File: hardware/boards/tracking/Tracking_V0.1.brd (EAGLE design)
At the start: 44 x 44 mm, 37 parts, among them J1 CON_HEADER_PRG_AVR_ICSP-PTH, U1 ATMEGA328P-AU, U3 USD-SOCKETNEW

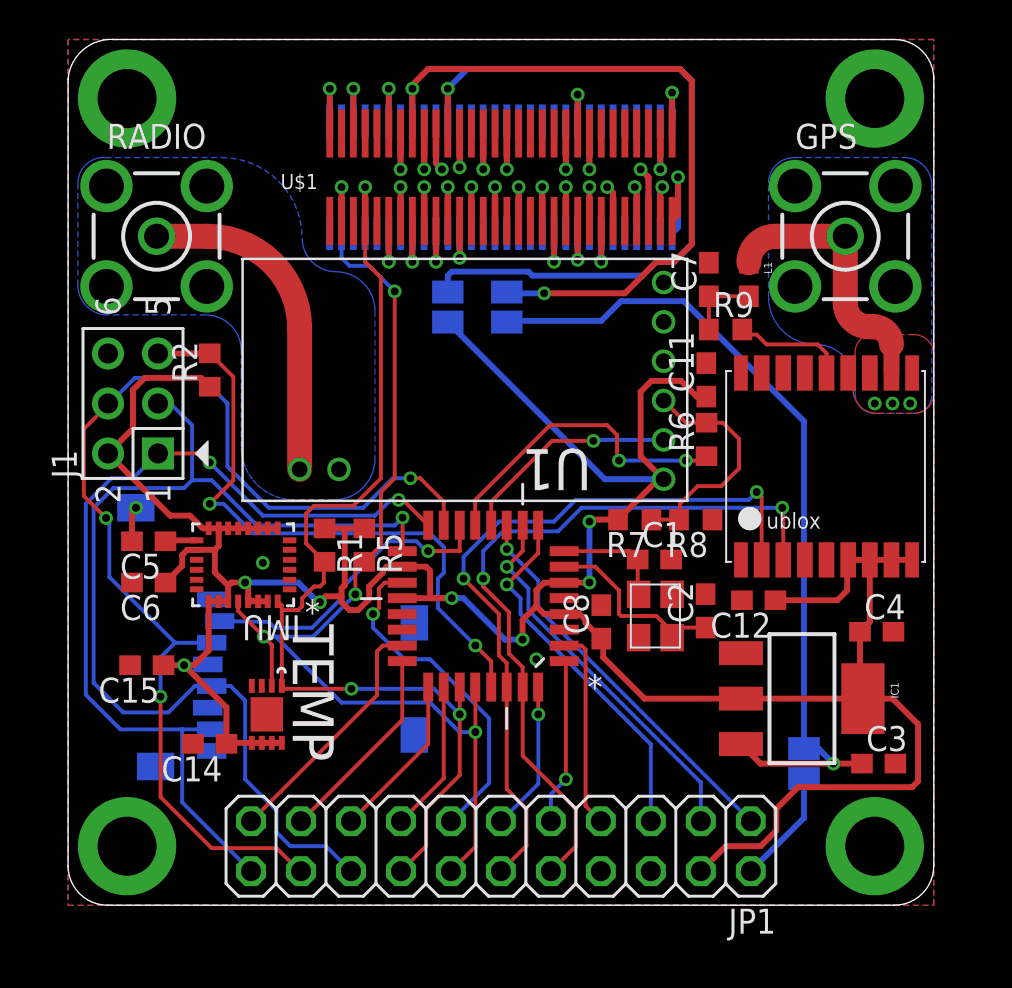
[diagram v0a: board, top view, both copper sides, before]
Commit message: Switched to right angle SMA connectors, created 3d render
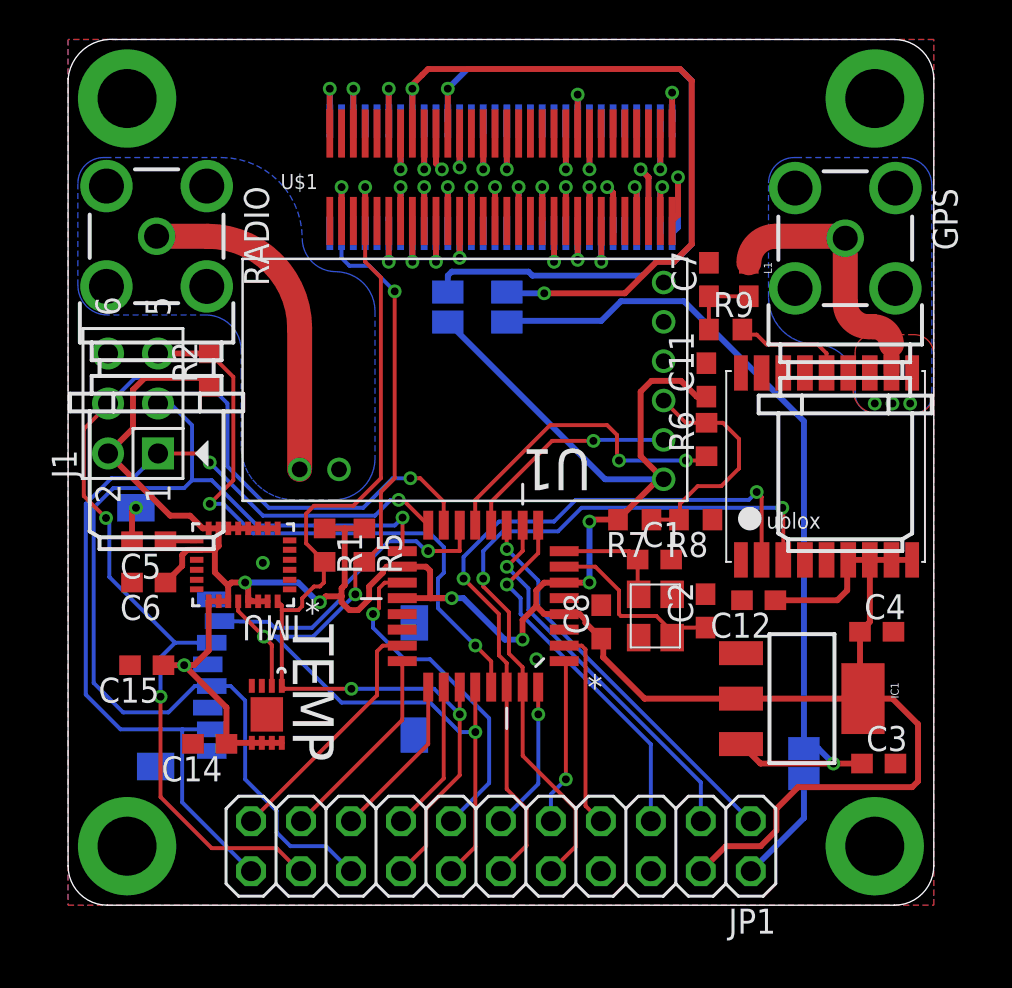
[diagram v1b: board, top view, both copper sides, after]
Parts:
- GPS, RADIO: value BU-SMA-V -> BU-SMA-G; device con-coax:BU-SMA-V -> con-coax:BU-SMA-G
- moved GPS 0.10 mm to (39.5, 33.9), turned to 270 degrees
- turned RADIO to 270 degrees
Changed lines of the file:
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@@
 <layer number="220" name="220bmp" color="21" fill="1" visible="no" active="no"/>
 <layer number="221" name="221bmp" color="22" fill="1" visible="no" active="no"/>
-<layer number="222" name="222bmp" color="23" fill="1" visible="no" active="no"/>
 <layer number="223" name="223bmp" color="24" fill="1" visible="no" active="no"/>
 <layer number="224" name="224bmp" color="25" fill="1" visible="no" active="no"/>
@@
 <element name="3.3V" library="jumper" package="SJ" value="" x="19.3" y="30.4" rot="MR90"/>
 <element name="U$4" library="Ava" package="UBLOX_MAX" value="UBLOX_MAX" x="38.6" y="22.5" rot="R270"/>
-<element name="GPS" library="con-coax" package="BU-SMA-V" value="BU-SMA-V" x="39.5" y="34">
-<attribute name="OC_NEWARK" value="unknown" x="31" y="36.3" size="1.778" layer="27" display="off"/>
-<attribute name="MPN" value="" x="31" y="36.3" size="1.778" layer="27" display="off"/>
-<attribute name="MF" value="" x="31" y="36.3" size="1.778" layer="27" display="off"/>
-<attribute name="OC_FARNELL" value="2144531" x="31" y="36.3" size="1.778" layer="27" display="off"/>
-</element>
 <element name="C12" library="rcl" package="C0603" value="100n" x="35.1" y="15.5" rot="R180">
 <attribute name="OC_FARNELL" value="2429362" x="55" y="13.3" size="1.778" layer="27" rot="R180" display="off"/>
@@
 <element name="L1" library="SparkFun" package="0603" value="33nH" x="34.6" y="31.8" rot="R270">
 <attribute name="OC_FARNELL" value="2285904" x="32.7" y="49.3" size="1.778" layer="27" rot="R270" display="off"/>
-</element>
-<element name="RADIO" library="con-coax" package="BU-SMA-V" value="BU-SMA-V" x="4.5" y="34">
-<attribute name="OC_NEWARK" value="unknown" x="-4" y="59" size="1.778" layer="27" display="off"/>
-<attribute name="MPN" value="" x="-4" y="59" size="1.778" layer="27" display="off"/>
-<attribute name="MF" value="" x="-4" y="59" size="1.778" layer="27" display="off"/>
-<attribute name="OC_FARNELL" value="2144531" x="-4" y="59" size="1.778" layer="27" display="off"/>
 </element>
 <element name="U$6" library="Ava" package="RADIOMETRIX-MTX2" value="RADIOMETRIX-MTX2" x="20.3" y="26.9"/>
@@
 <element name="LOCAL" library="jumper" package="SJ" value="" x="37.4" y="7.2" rot="MR270"/>
 <element name="JP1" library="pinhead" package="2X11" value="" x="22" y="3" rot="R180"/>
+<element name="GPS" library="con-coax" package="BU-SMA-G" value="BU-SMA-G" x="39.5" y="33.9" rot="R270">
+<attribute name="OC_NEWARK" value="unknown" x="39.5" y="33.9" size="1.778" layer="27" rot="R270" display="off"/>
+<attribute name="MPN" value="" x="39.5" y="33.9" size="1.778" layer="27" rot="R270" display="off"/>
+<attribute name="MF" value="" x="39.5" y="33.9" size="1.778" layer="27" rot="R270" display="off"/>
+<attribute name="OC_FARNELL" value="unknown" x="39.5" y="33.9" size="1.778" layer="27" rot="R270" display="off"/>
+</element>
+<element name="RADIO" library="con-coax" package="BU-SMA-G" value="BU-SMA-G" x="4.5" y="34" rot="R270">
+<attribute name="OC_NEWARK" value="unknown" x="4.5" y="34" size="1.778" layer="27" rot="R270" display="off"/>
+<attribute name="MPN" value="" x="4.5" y="34" size="1.778" layer="27" rot="R270" display="off"/>
+<attribute name="MF" value="" x="4.5" y="34" size="1.778" layer="27" rot="R270" display="off"/>
+<attribute name="OC_FARNELL" value="unknown" x="4.5" y="34" size="1.778" layer="27" rot="R270" display="off"/>
+</element>
 </elements>
 <signals>
@@
 <contactref element="U$4" pad="10_GND"/>
 <contactref element="U$4" pad="12_GND"/>
-<contactref element="GPS" pad="3"/>
-<contactref element="GPS" pad="5"/>
-<contactref element="GPS" pad="2"/>
-<contactref element="GPS" pad="4"/>
 <contactref element="C7" pad="2"/>
 <contactref element="U$6" pad="GND"/>
@@
 <via x="41.9" y="25.5" extent="1-16" drill="0.4"/>
 <via x="42.8" y="25.5" extent="1-16" drill="0.4"/>
-<polygon width="0.2" layer="1" thermals="no" rank="2">
+<polygon width="0.2" layer="1" rank="2">
 <vertex x="0" y="0"/>
 <vertex x="44" y="0"/>
@@
 <vertex x="0" y="44"/>
 </polygon>
-<polygon width="0.2" layer="16" thermals="no" rank="2">
+<polygon width="0.2" layer="16" rank="2">
 <vertex x="0" y="0"/>
 <vertex x="44" y="0"/>
@@
 <wire x1="3.45" y1="20.2" x2="2.8" y2="20.2" width="0.3" layer="16"/>
 <via x="23.8" y="12.5" extent="1-16" drill="0.4"/>
+<contactref element="GPS" pad="5"/>
+<contactref element="GPS" pad="3"/>
+<contactref element="GPS" pad="2"/>
+<contactref element="GPS" pad="4"/>
+<wire x1="25.2148" y1="14.0062" x2="25.2148" y2="15.6064" width="0" layer="19" extent="1-1"/>
+<wire x1="14.5" y1="34.15" x2="14.5" y2="34.775" width="0" layer="19" extent="1-16"/>
+<wire x1="28.3" y1="34.15" x2="28.3" y2="34.775" width="0" layer="19" extent="1-16"/>
+<wire x1="15.7" y1="34.775" x2="15.7" y2="34.15" width="0" layer="19" extent="1-16"/>
+<wire x1="16.9852" y1="14.7936" x2="17.6" y2="14.35" width="0" layer="19" extent="1-16"/>
+<wire x1="27.1" y1="15.25" x2="25.2148" y2="15.6064" width="0" layer="19" extent="1-1"/>
 </signal>
 <signal name="VBUS_SW3">
@@
 <signal name="N$1">
 <contactref element="U$4" pad="11_RF_IN"/>
-<contactref element="GPS" pad="1"/>
 <contactref element="L1" pad="1"/>
-<wire x1="39.5" y1="34" x2="39.5" y2="30.6" width="1.27" layer="1"/>
 <wire x1="39.5" y1="30.6" x2="40.7" y2="29.4" width="1.27" layer="1" curve="90"/>
 <wire x1="40.7" y1="29.4" x2="40.94" y2="29.4" width="1.27" layer="1"/>
@@
 <wire x1="41.85" y1="28.49" x2="41.85" y2="27.05" width="0.8" layer="1"/>
 <wire x1="34.6" y1="32.65" x2="35.95" y2="34" width="1.27" layer="1" curve="-90"/>
+<contactref element="GPS" pad="1"/>
 <wire x1="35.95" y1="34" x2="39.5" y2="34" width="1.27" layer="1"/>
+<wire x1="39.5" y1="34" x2="39.5" y2="33.9" width="1.27" layer="1"/>
+<wire x1="39.5" y1="33.9" x2="39.5" y2="30.6" width="1.27" layer="1"/>
 </signal>
 <signal name="N$3">
@@
 </signal>
 <signal name="RFGND">
-<contactref element="RADIO" pad="3"/>
-<contactref element="RADIO" pad="5"/>
-<contactref element="RADIO" pad="2"/>
-<contactref element="RADIO" pad="4"/>
 <contactref element="U$6" pad="RFGND"/>
 <polygon width="0.2" layer="16" isolate="0.254" thermals="no">
@@
 <vertex x="1.8" y="38"/>
 </polygon>
+<contactref element="RADIO" pad="5"/>
+<contactref element="RADIO" pad="3"/>
+<contactref element="RADIO" pad="2"/>
+<contactref element="RADIO" pad="4"/>
 </signal>
 <signal name="N$6">
-<contactref element="RADIO" pad="1"/>
 <contactref element="U$6" pad="RF"/>
-<wire x1="4.5" y1="34" x2="7.1" y2="34" width="1.27" layer="1"/>
 <wire x1="7.1" y1="34" x2="11.77" y2="29.33" width="1.27" layer="1" curve="-90"/>
 <wire x1="11.77" y1="29.33" x2="11.77" y2="22.15" width="1.27" layer="1"/>
+<contactref element="RADIO" pad="1"/>
+<wire x1="7.1" y1="34" x2="4.5" y2="34" width="1.27" layer="1"/>
 </signal>
 <signal name="N$7">
